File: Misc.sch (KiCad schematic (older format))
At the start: 18 parts, among them U3 PCF8523TK, U4 TLV70218DBV, U5 CDCE913PW, U7 LM75BDP, U8 LM75BDP, X1 32768, X2 20MHz

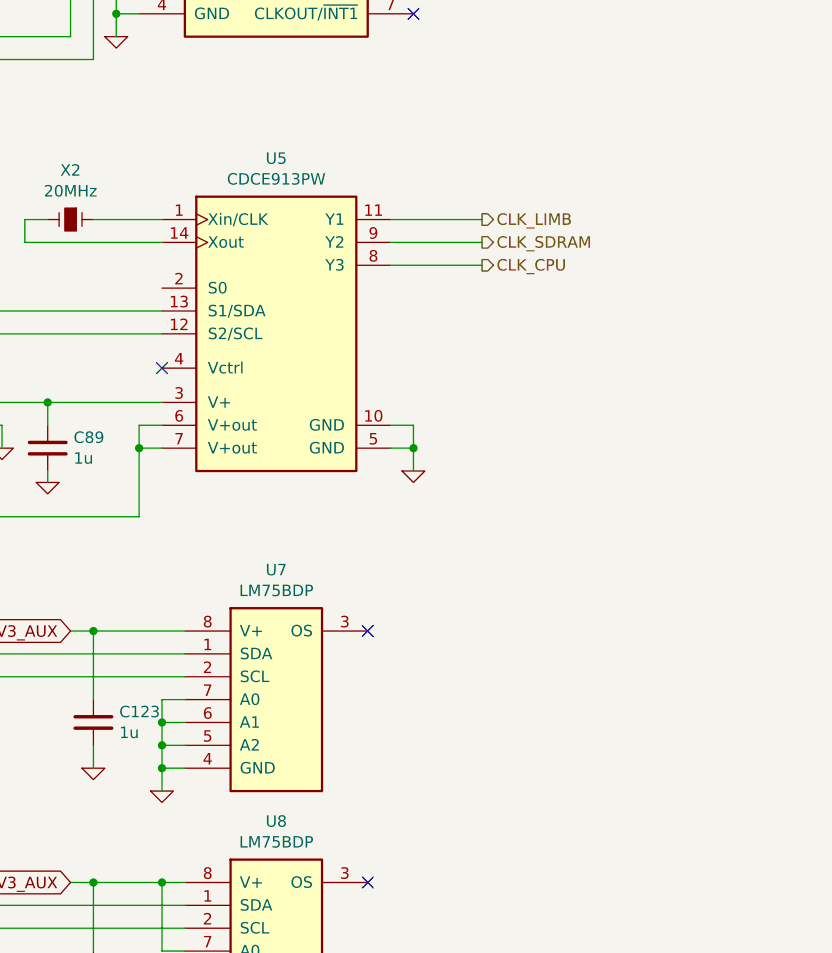
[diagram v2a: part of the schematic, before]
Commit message: Route clocks
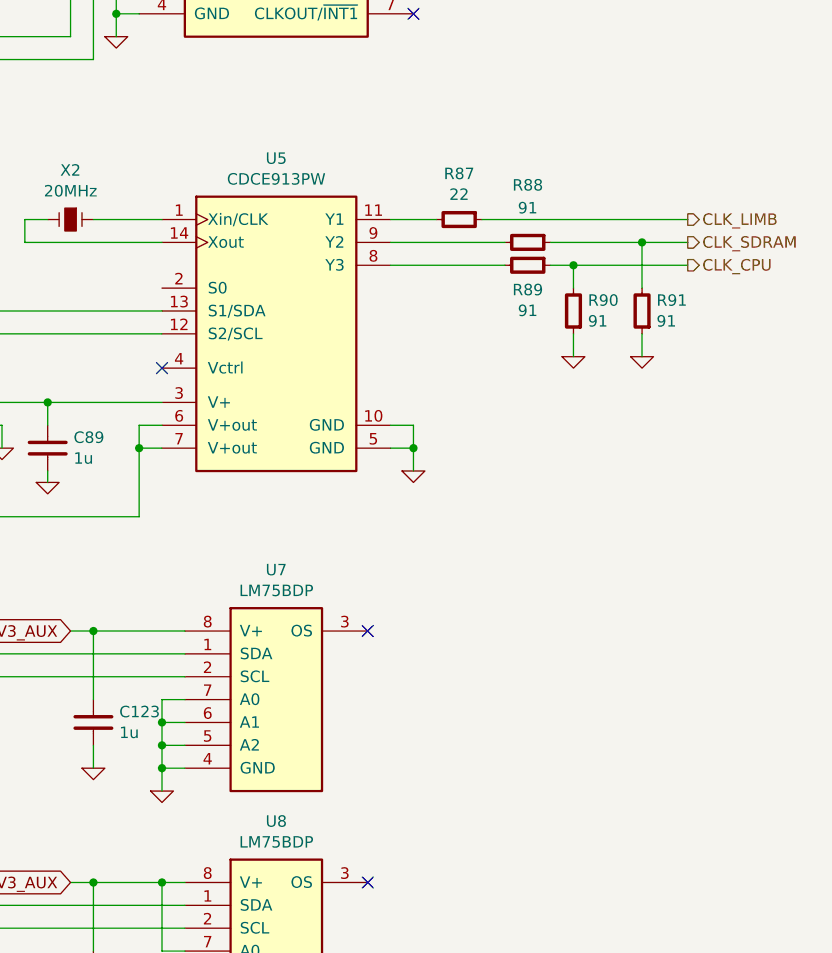
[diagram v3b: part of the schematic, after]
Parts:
- added R87: 22, IPC7351-Nominal:RESC1005X40, symbol R-0402
- added R88, R89, R90, R91: 91, IPC7351-Nominal:RESC1005X40, symbol R-0402
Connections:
- net CLK_CPU: now also R89.1, R90.2; no longer U5.8 (Y3)
- net CLK_LIMB: now also R87.1; no longer U5.11 (Y1)
- net CLK_SDRAM: now also R88.1, R91.2; no longer U5.9 (Y2)
- net GND: now also R90.1, R91.1
- new net: R87.2, U5.11 (Y1)
- new net: R89.2, U5.8 (Y3)
- new net: R88.2, U5.9 (Y2)
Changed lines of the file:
@@
 $Descr A4 11693 8268
 encoding utf-8
-Sheet 10 10
+Sheet 9 10
 Title ""
 Date ""
@@
 Connection ~ 4900 2100
 $Comp
-L GND #PWR176
+L GND #PWR174
 U 1 1 57981F37
 P 4900 2200
-F 0 "#PWR176" H 4900 2200 30  0001 C CNN
+F 0 "#PWR174" H 4900 2200 30  0001 C CNN
 F 1 "GND" H 4900 2130 30  0001 C CNN
 F 2 "" H 4900 2200 60  0000 C CNN
@@
 	6700 1500 6700 1600
 $Comp
-L GND #PWR180
+L GND #PWR178
 U 1 1 57983039
 P 6850 1700
-F 0 "#PWR180" H 6850 1700 30  0001 C CNN
+F 0 "#PWR178" H 6850 1700 30  0001 C CNN
 F 1 "GND" H 6850 1630 30  0001 C CNN
 F 2 "" H 6850 1700 60  0000 C CNN
@@
 Connection ~ 2100 1500
 $Comp
-L GND #PWR164
+L GND #PWR162
 U 1 1 57985104
 P 2100 1850
-F 0 "#PWR164" H 2100 1850 30  0001 C CNN
+F 0 "#PWR162" H 2100 1850 30  0001 C CNN
 F 1 "GND" H 2100 1780 30  0001 C CNN
 F 2 "" H 2100 1850 60  0000 C CNN
@@
 	2100 1850 2100 1800
 $Comp
-L GND #PWR165
+L GND #PWR163
 U 1 1 57985148
 P 2450 1850
-F 0 "#PWR165" H 2450 1850 30  0001 C CNN
+F 0 "#PWR163" H 2450 1850 30  0001 C CNN
 F 1 "GND" H 2450 1780 30  0001 C CNN
 F 2 "" H 2450 1850 60  0000 C CNN
@@
 	2450 1850 2450 1800
 $Comp
-L GND #PWR166
+L GND #PWR164
 U 1 1 5798515D
 P 2800 1850
-F 0 "#PWR166" H 2800 1850 30  0001 C CNN
+F 0 "#PWR164" H 2800 1850 30  0001 C CNN
 F 1 "GND" H 2800 1780 30  0001 C CNN
 F 2 "" H 2800 1850 60  0000 C CNN
@@
 	2800 1850 2800 1800
 $Comp
-L GND #PWR168
+L GND #PWR166
 U 1 1 57985164
 P 3150 1850
-F 0 "#PWR168" H 3150 1850 30  0001 C CNN
+F 0 "#PWR166" H 3150 1850 30  0001 C CNN
 F 1 "GND" H 3150 1780 30  0001 C CNN
 F 2 "" H 3150 1850 60  0000 C CNN
@@
 	3800 1600 3800 1700
 $Comp
-L GND #PWR170
+L GND #PWR168
 U 1 1 5798538F
 P 3800 2000
-F 0 "#PWR170" H 3800 2000 30  0001 C CNN
+F 0 "#PWR168" H 3800 2000 30  0001 C CNN
 F 1 "GND" H 3800 1930 30  0001 C CNN
 F 2 "" H 3800 2000 60  0000 C CNN
@@
 Connection ~ 4300 1600
 $Comp
-L GND #PWR171
+L GND #PWR169
 U 1 1 5798545A
 P 4300 2000
-F 0 "#PWR171" H 4300 2000 30  0001 C CNN
+F 0 "#PWR169" H 4300 2000 30  0001 C CNN
 F 1 "GND" H 4300 1930 30  0001 C CNN
 F 2 "" H 4300 2000 60  0000 C CNN
@@
 	1    0    0    -1
 $EndComp
-Text HLabel 6500 3000 2    50   Output ~ 0
+Text HLabel 7400 3000 2    50   Output ~ 0
 CLK_LIMB
-Text HLabel 6500 3100 2    50   Output ~ 0
+Text HLabel 7400 3100 2    50   Output ~ 0
 CLK_SDRAM
-Text HLabel 6500 3200 2    50   Output ~ 0
+Text HLabel 7400 3200 2    50   Output ~ 0
 CLK_CPU
-Wire Wire Line
-	6500 3000 6100 3000
-Wire Wire Line
-	6500 3100 6100 3100
-Wire Wire Line
-	6500 3200 6100 3200
-$Comp
-L GND #PWR179
+$Comp
+L GND #PWR177
 U 1 1 5798C21D
 P 6200 4100
-F 0 "#PWR179" H 6200 4100 30  0001 C CNN
+F 0 "#PWR177" H 6200 4100 30  0001 C CNN
 F 1 "GND" H 6200 4030 30  0001 C CNN
 F 2 "" H 6200 4100 60  0000 C CNN
@@
 	4300 3800 5100 3800
 $Comp
-L GND #PWR172
+L GND #PWR170
 U 1 1 5798C570
 P 4400 4000
-F 0 "#PWR172" H 4400 4000 30  0001 C CNN
+F 0 "#PWR170" H 4400 4000 30  0001 C CNN
 F 1 "GND" H 4400 3930 30  0001 C CNN
 F 2 "" H 4400 4000 60  0000 C CNN
@@
 	4400 3900 4300 3900
 $Comp
-L GND #PWR169
+L GND #PWR167
 U 1 1 5798C5E9
 P 3500 4100
-F 0 "#PWR169" H 3500 4100 30  0001 C CNN
+F 0 "#PWR167" H 3500 4100 30  0001 C CNN
 F 1 "GND" H 3500 4030 30  0001 C CNN
 F 2 "" H 3500 4100 60  0000 C CNN
@@
 Connection ~ 3100 3800
 $Comp
-L GND #PWR167
+L GND #PWR165
 U 1 1 5798C8CA
 P 3100 4150
-F 0 "#PWR167" H 3100 4150 30  0001 C CNN
+F 0 "#PWR165" H 3100 4150 30  0001 C CNN
 F 1 "GND" H 3100 4080 30  0001 C CNN
 F 2 "" H 3100 4150 60  0000 C CNN
@@
 Connection ~ 4600 3800
 $Comp
-L GND #PWR173
+L GND #PWR171
 U 1 1 5798C9F9
 P 4600 4150
-F 0 "#PWR173" H 4600 4150 30  0001 C CNN
+F 0 "#PWR171" H 4600 4150 30  0001 C CNN
 F 1 "GND" H 4600 4080 30  0001 C CNN
 F 2 "" H 4600 4150 60  0000 C CNN
@@
 Connection ~ 2300 3500
 $Comp
-L GND #PWR177
+L GND #PWR175
 U 1 1 579F4E8E
 P 5100 5500
-F 0 "#PWR177" H 5100 5500 30  0001 C CNN
+F 0 "#PWR175" H 5100 5500 30  0001 C CNN
 F 1 "GND" H 5100 5430 30  0001 C CNN
 F 2 "" H 5100 5500 60  0000 C CNN
@@
 $EndComp
 Wire Wire Line
-	5100 5500 5100 5100
+	5100 5100 5100 5500
 Wire Wire Line
 	5100 5100 5200 5100
@@
 	5100 6300 5100 6600
 $Comp
-L GND #PWR178
+L GND #PWR176
 U 1 1 579F532E
 P 5100 6600
-F 0 "#PWR178" H 5100 6600 30  0001 C CNN
+F 0 "#PWR176" H 5100 6600 30  0001 C CNN
 F 1 "GND" H 5100 6530 30  0001 C CNN
 F 2 "" H 5100 6600 60  0000 C CNN
@@
 Connection ~ 4800 4800
 $Comp
-L GND #PWR174
+L GND #PWR172
 U 1 1 579F5F9F
 P 4800 5400
-F 0 "#PWR174" H 4800 5400 30  0001 C CNN
+F 0 "#PWR172" H 4800 5400 30  0001 C CNN
 F 1 "GND" H 4800 5330 30  0001 C CNN
 F 2 "" H 4800 5400 60  0000 C CNN
@@
 Connection ~ 4800 5900
 $Comp
-L GND #PWR175
+L GND #PWR173
 U 1 1 579F6133
 P 4800 6500
-F 0 "#PWR175" H 4800 6500 30  0001 C CNN
+F 0 "#PWR173" H 4800 6500 30  0001 C CNN
 F 1 "GND" H 4800 6430 30  0001 C CNN
 F 2 "" H 4800 6500 60  0000 C CNN
@@
 Wire Wire Line
 	4800 6500 4800 6400
+$Comp
+L R-0402 R87
+U 1 1 57A14DBD
+P 6400 3000
+F 0 "R87" V 6200 3000 50  0000 C CNN
+F 1 "22" V 6291 3000 50  0000 C CNN
+F 2 "IPC7351-Nominal:RESC1005X40" H 6400 3000 50  0001 C CNN
+F 3 "" H 6400 3050 60  0000 C CNN
+F 4 "RES SMD 22 1% [0402]" H 7150 3550 60  0001 C CNN "BOM"
+	1    6400 3000
+	0    1    1    0
+$EndComp
+Wire Wire Line
+	6300 3000 6100 3000
+Wire Wire Line
+	6500 3000 7400 3000
+$Comp
+L R-0402 R88
+U 1 1 57A1503E
+P 6700 3100
+F 0 "R88" V 6450 3100 50  0000 C CNN
+F 1 "91" V 6550 3100 50  0000 C CNN
+F 2 "IPC7351-Nominal:RESC1005X40" H 6700 3100 50  0001 C CNN
+F 3 "" H 6700 3150 60  0000 C CNN
+F 4 "RES SMD 91 1% [0402]" H 7450 3650 60  0001 C CNN "BOM"
+	1    6700 3100
+	0    1    1    0
+$EndComp
+Wire Wire Line
+	6600 3100 6100 3100
+Wire Wire Line
+	6800 3100 7400 3100
+$Comp
+L R-0402 R89
+U 1 1 57A152BE
+P 6700 3200
+F 0 "R89" V 6808 3200 50  0000 C CNN
+F 1 "91" V 6899 3200 50  0000 C CNN
+F 2 "IPC7351-Nominal:RESC1005X40" H 6700 3200 50  0001 C CNN
+F 3 "" H 6700 3250 60  0000 C CNN
+F 4 "RES SMD 91 1% [0402]" H 7450 3750 60  0001 C CNN "BOM"
+	1    6700 3200
+	0    1    1    0
+$EndComp
+Wire Wire Line
+	6800 3200 7400 3200
+Wire Wire Line
+	6600 3200 6100 3200
+$Comp
+L R-0402 R90
+U 1 1 57A154AF
+P 6900 3400
+F 0 "R90" H 6837 3354 50  0000 R CNN
+F 1 "91" H 6837 3445 50  0000 R CNN
+F 2 "IPC7351-Nominal:RESC1005X40" H 6900 3400 50  0001 C CNN
+F 3 "" H 6900 3450 60  0000 C CNN
+F 4 "RES SMD 91 1% [0402]" H 7650 3950 60  0001 C CNN "BOM"
+	1    6900 3400
+	-1   0    0    1
+$EndComp
+Wire Wire Line
+	6900 3300 6900 3200
+Connection ~ 6900 3200
+$Comp
+L R-0402 R91
+U 1 1 57A15674
+P 7200 3400
+F 0 "R91" H 7137 3354 50  0000 R CNN
+F 1 "91" H 7137 3445 50  0000 R CNN
+F 2 "IPC7351-Nominal:RESC1005X40" H 7200 3400 50  0001 C CNN
+F 3 "" H 7200 3450 60  0000 C CNN
+F 4 "RES SMD 91 1% [0402]" H 7950 3950 60  0001 C CNN "BOM"
+	1    7200 3400
+	-1   0    0    1
+$EndComp
+Wire Wire Line
+	7200 3300 7200 3100
+Connection ~ 7200 3100
+$Comp
+L GND #PWR179
+U 1 1 57A157A8
+P 6900 3600
+F 0 "#PWR179" H 6900 3600 30  0001 C CNN
+F 1 "GND" H 6900 3530 30  0001 C CNN
+F 2 "" H 6900 3600 60  0000 C CNN
+F 3 "" H 6900 3600 60  0000 C CNN
+	1    6900 3600
+	1    0    0    -1
+$EndComp
+Wire Wire Line
+	6900 3600 6900 3500
+$Comp
+L GND #PWR180
+U 1 1 57A158A4
+P 7200 3600
+F 0 "#PWR180" H 7200 3600 30  0001 C CNN
+F 1 "GND" H 7200 3530 30  0001 C CNN
+F 2 "" H 7200 3600 60  0000 C CNN
+F 3 "" H 7200 3600 60  0000 C CNN
+	1    7200 3600
+	1    0    0    -1
+$EndComp
+Wire Wire Line
+	7200 3600 7200 3500
 $EndSCHEMATC

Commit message: Proper coin cell holder
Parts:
- BT1: footprint (none) -> manuf:MPD-BU2032SM-HD-G
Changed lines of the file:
@@
 F 0 "BT1" H 3940 1821 50  0000 L CNN
 F 1 "3V" H 3940 1730 50  0000 L CNN
-F 2 "" H 3800 1700 60  0000 C CNN
+F 2 "manuf:MPD-BU2032SM-HD-G" H 3800 1700 60  0001 C CNN
 F 3 "" H 3800 1700 60  0000 C CNN
 F 4 "DIST DIGIKEY BU2032SM-HD-GCT-ND" H 3800 1800 60  0001 C CNN "BOM"

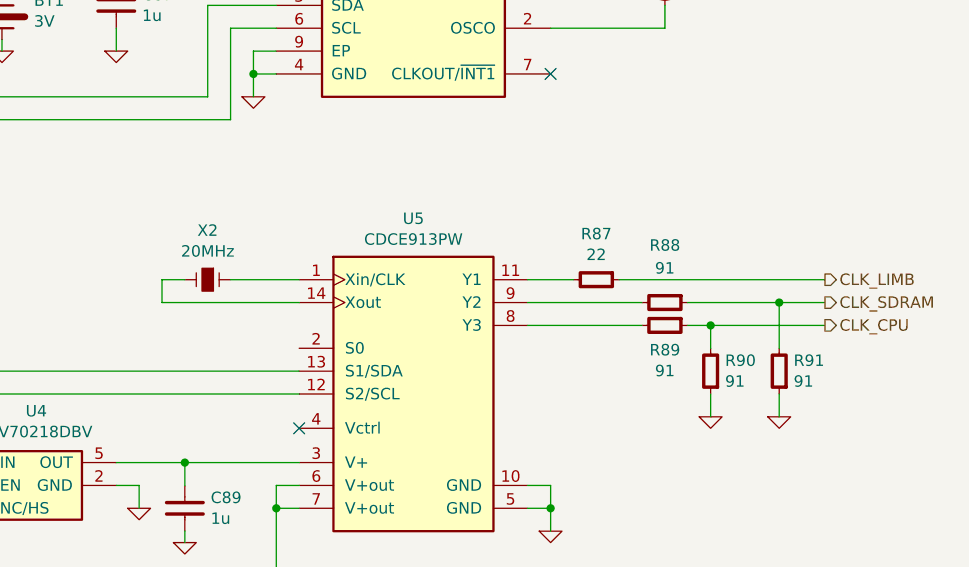
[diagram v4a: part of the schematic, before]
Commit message: Add RS-232
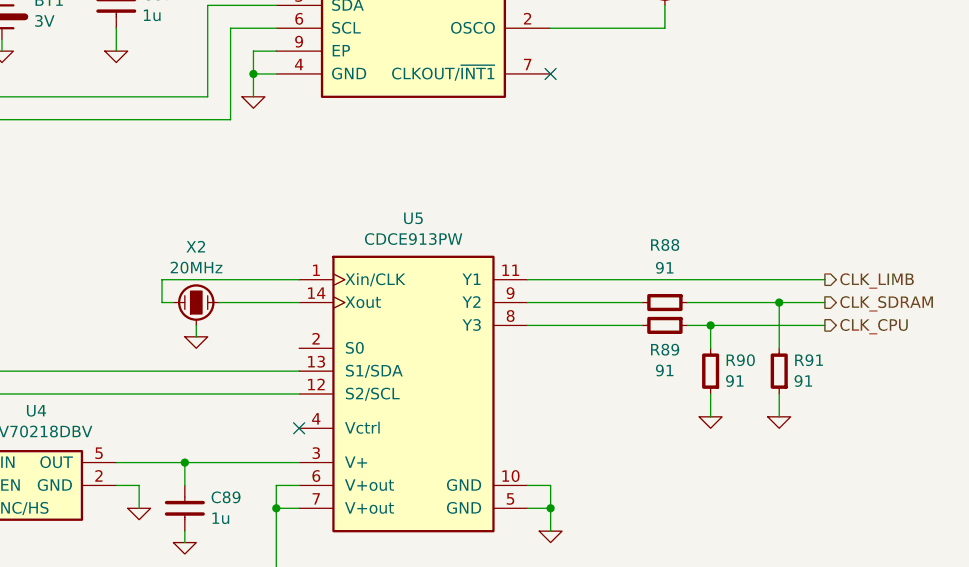
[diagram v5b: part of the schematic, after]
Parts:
- removed R87: 22, IPC7351-Nominal:RESC1005X40, symbol R-0402
- removed X2: 20MHz, IPC7351-Nominal:XTAL1200X480X460, symbol XTAL-HC49US-SMD
- added X2: 20MHz, manuf:ABRACON-ABM8G, symbol XTAL-ABRACON-ABM8G
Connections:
- net CLK_LIMB: now also U5.11 (Y1)
- net GND: now also X2.3
- net at U5.1 (Xin/CLK): now also X2.1
- net at U5.14 (Xout): now also X2.2
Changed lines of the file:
@@
 Connection ~ 4900 2100
 $Comp
-L GND #PWR174
+L GND #PWR183
 U 1 1 57981F37
 P 4900 2200
-F 0 "#PWR174" H 4900 2200 30  0001 C CNN
+F 0 "#PWR183" H 4900 2200 30  0001 C CNN
 F 1 "GND" H 4900 2130 30  0001 C CNN
 F 2 "" H 4900 2200 60  0000 C CNN
@@
 	6700 1500 6700 1600
 $Comp
-L GND #PWR178
+L GND #PWR187
 U 1 1 57983039
 P 6850 1700
-F 0 "#PWR178" H 6850 1700 30  0001 C CNN
+F 0 "#PWR187" H 6850 1700 30  0001 C CNN
 F 1 "GND" H 6850 1630 30  0001 C CNN
 F 2 "" H 6850 1700 60  0000 C CNN
@@
 Connection ~ 2100 1500
 $Comp
-L GND #PWR162
+L GND #PWR170
 U 1 1 57985104
 P 2100 1850
-F 0 "#PWR162" H 2100 1850 30  0001 C CNN
+F 0 "#PWR170" H 2100 1850 30  0001 C CNN
 F 1 "GND" H 2100 1780 30  0001 C CNN
 F 2 "" H 2100 1850 60  0000 C CNN
@@
 	2100 1850 2100 1800
 $Comp
-L GND #PWR163
+L GND #PWR171
 U 1 1 57985148
 P 2450 1850
-F 0 "#PWR163" H 2450 1850 30  0001 C CNN
+F 0 "#PWR171" H 2450 1850 30  0001 C CNN
 F 1 "GND" H 2450 1780 30  0001 C CNN
 F 2 "" H 2450 1850 60  0000 C CNN
@@
 	2450 1850 2450 1800
 $Comp
-L GND #PWR164
+L GND #PWR172
 U 1 1 5798515D
 P 2800 1850
-F 0 "#PWR164" H 2800 1850 30  0001 C CNN
+F 0 "#PWR172" H 2800 1850 30  0001 C CNN
 F 1 "GND" H 2800 1780 30  0001 C CNN
 F 2 "" H 2800 1850 60  0000 C CNN
@@
 	2800 1850 2800 1800
 $Comp
-L GND #PWR166
+L GND #PWR174
 U 1 1 57985164
 P 3150 1850
-F 0 "#PWR166" H 3150 1850 30  0001 C CNN
+F 0 "#PWR174" H 3150 1850 30  0001 C CNN
 F 1 "GND" H 3150 1780 30  0001 C CNN
 F 2 "" H 3150 1850 60  0000 C CNN
@@
 	3800 1600 3800 1700
 $Comp
-L GND #PWR168
+L GND #PWR176
 U 1 1 5798538F
 P 3800 2000
-F 0 "#PWR168" H 3800 2000 30  0001 C CNN
+F 0 "#PWR176" H 3800 2000 30  0001 C CNN
 F 1 "GND" H 3800 1930 30  0001 C CNN
 F 2 "" H 3800 2000 60  0000 C CNN
@@
 Connection ~ 4300 1600
 $Comp
-L GND #PWR169
+L GND #PWR177
 U 1 1 5798545A
 P 4300 2000
-F 0 "#PWR169" H 4300 2000 30  0001 C CNN
+F 0 "#PWR177" H 4300 2000 30  0001 C CNN
 F 1 "GND" H 4300 1930 30  0001 C CNN
 F 2 "" H 4300 2000 60  0000 C CNN
@@
 CLK_CPU
 $Comp
-L GND #PWR177
+L GND #PWR186
 U 1 1 5798C21D
 P 6200 4100
-F 0 "#PWR177" H 6200 4100 30  0001 C CNN
+F 0 "#PWR186" H 6200 4100 30  0001 C CNN
 F 1 "GND" H 6200 4030 30  0001 C CNN
 F 2 "" H 6200 4100 60  0000 C CNN
@@
 	6200 4000 6100 4000
 Connection ~ 6200 4000
-$Comp
-L XTAL-HC49US-SMD X2
-U 1 1 5798C2EB
-P 4700 3000
-F 0 "X2" V 4485 3000 50  0000 C CNN
-F 1 "20MHz" V 4576 3000 50  0000 C CNN
-F 2 "IPC7351-Nominal:XTAL1200X480X460" H 4800 2950 60  0001 C CNN
-F 3 "" H 4700 3000 60  0000 C CNN
-	1    4700 3000
-	0    1    1    0
-$EndComp
-Wire Wire Line
-	4800 3000 5100 3000
-Wire Wire Line
-	5100 3100 4500 3100
 Wire Wire Line
 	4500 3100 4500 3000
 Wire Wire Line
-	4500 3000 4600 3000
+	4500 3000 5100 3000
 Wire Wire Line
 	2400 3400 5100 3400
@@
 	4300 3800 5100 3800
 $Comp
-L GND #PWR170
+L GND #PWR178
 U 1 1 5798C570
 P 4400 4000
-F 0 "#PWR170" H 4400 4000 30  0001 C CNN
+F 0 "#PWR178" H 4400 4000 30  0001 C CNN
 F 1 "GND" H 4400 3930 30  0001 C CNN
 F 2 "" H 4400 4000 60  0000 C CNN
@@
 	4400 3900 4300 3900
 $Comp
-L GND #PWR167
+L GND #PWR175
 U 1 1 5798C5E9
 P 3500 4100
-F 0 "#PWR167" H 3500 4100 30  0001 C CNN
+F 0 "#PWR175" H 3500 4100 30  0001 C CNN
 F 1 "GND" H 3500 4030 30  0001 C CNN
 F 2 "" H 3500 4100 60  0000 C CNN
@@
 Connection ~ 3100 3800
 $Comp
-L GND #PWR165
+L GND #PWR173
 U 1 1 5798C8CA
 P 3100 4150
-F 0 "#PWR165" H 3100 4150 30  0001 C CNN
+F 0 "#PWR173" H 3100 4150 30  0001 C CNN
 F 1 "GND" H 3100 4080 30  0001 C CNN
 F 2 "" H 3100 4150 60  0000 C CNN
@@
 Connection ~ 4600 3800
 $Comp
-L GND #PWR171
+L GND #PWR179
 U 1 1 5798C9F9
 P 4600 4150
-F 0 "#PWR171" H 4600 4150 30  0001 C CNN
+F 0 "#PWR179" H 4600 4150 30  0001 C CNN
 F 1 "GND" H 4600 4080 30  0001 C CNN
 F 2 "" H 4600 4150 60  0000 C CNN
@@
 Connection ~ 2300 3500
 $Comp
-L GND #PWR175
+L GND #PWR184
 U 1 1 579F4E8E
 P 5100 5500
-F 0 "#PWR175" H 5100 5500 30  0001 C CNN
+F 0 "#PWR184" H 5100 5500 30  0001 C CNN
 F 1 "GND" H 5100 5430 30  0001 C CNN
 F 2 "" H 5100 5500 60  0000 C CNN
@@
 	5100 6300 5100 6600
 $Comp
-L GND #PWR176
+L GND #PWR185
 U 1 1 579F532E
 P 5100 6600
-F 0 "#PWR176" H 5100 6600 30  0001 C CNN
+F 0 "#PWR185" H 5100 6600 30  0001 C CNN
 F 1 "GND" H 5100 6530 30  0001 C CNN
 F 2 "" H 5100 6600 60  0000 C CNN
@@
 Connection ~ 4800 4800
 $Comp
-L GND #PWR172
+L GND #PWR181
 U 1 1 579F5F9F
 P 4800 5400
-F 0 "#PWR172" H 4800 5400 30  0001 C CNN
+F 0 "#PWR181" H 4800 5400 30  0001 C CNN
 F 1 "GND" H 4800 5330 30  0001 C CNN
 F 2 "" H 4800 5400 60  0000 C CNN
@@
 Connection ~ 4800 5900
 $Comp
-L GND #PWR173
+L GND #PWR182
 U 1 1 579F6133
 P 4800 6500
-F 0 "#PWR173" H 4800 6500 30  0001 C CNN
+F 0 "#PWR182" H 4800 6500 30  0001 C CNN
 F 1 "GND" H 4800 6430 30  0001 C CNN
 F 2 "" H 4800 6500 60  0000 C CNN
@@
 Wire Wire Line
 	4800 6500 4800 6400
-$Comp
-L R-0402 R87
-U 1 1 57A14DBD
-P 6400 3000
-F 0 "R87" V 6200 3000 50  0000 C CNN
-F 1 "22" V 6291 3000 50  0000 C CNN
-F 2 "IPC7351-Nominal:RESC1005X40" H 6400 3000 50  0001 C CNN
-F 3 "" H 6400 3050 60  0000 C CNN
-F 4 "RES SMD 22 1% [0402]" H 7150 3550 60  0001 C CNN "BOM"
-	1    6400 3000
-	0    1    1    0
-$EndComp
-Wire Wire Line
-	6300 3000 6100 3000
-Wire Wire Line
-	6500 3000 7400 3000
+Wire Wire Line
+	6100 3000 7400 3000
 $Comp
 L R-0402 R88
@@
 Connection ~ 7200 3100
 $Comp
-L GND #PWR179
+L GND #PWR188
 U 1 1 57A157A8
 P 6900 3600
-F 0 "#PWR179" H 6900 3600 30  0001 C CNN
+F 0 "#PWR188" H 6900 3600 30  0001 C CNN
 F 1 "GND" H 6900 3530 30  0001 C CNN
 F 2 "" H 6900 3600 60  0000 C CNN
@@
 	6900 3600 6900 3500
 $Comp
-L GND #PWR180
+L GND #PWR189
 U 1 1 57A158A4
 P 7200 3600
-F 0 "#PWR180" H 7200 3600 30  0001 C CNN
+F 0 "#PWR189" H 7200 3600 30  0001 C CNN
 F 1 "GND" H 7200 3530 30  0001 C CNN
 F 2 "" H 7200 3600 60  0000 C CNN
@@
 Wire Wire Line
 	7200 3600 7200 3500
+$Comp
+L XTAL-ABRACON-ABM8G X2
+U 1 1 57A1738B
+P 4650 3100
+F 0 "X2" V 4892 3100 50  0000 C CNN
+F 1 "20MHz" V 4801 3100 50  0000 C CNN
+F 2 "manuf:ABRACON-ABM8G" H 4650 2950 60  0001 C CNN
+F 3 "http://www.abracon.com/Resonators/ABM8G.pdf" H 4650 3100 50  0001 C CNN
+F 4 "DIST DIGIKEY 535-10271-1-ND" H 4650 3100 60  0001 C CNN "BOM"
+	1    4650 3100
+	0    -1   -1   0
+$EndComp
+Wire Wire Line
+	4550 3100 4500 3100
+Wire Wire Line
+	4750 3100 5100 3100
+$Comp
+L GND #PWR180
+U 1 1 57A177C2
+P 4650 3250
+F 0 "#PWR180" H 4650 3250 30  0001 C CNN
+F 1 "GND" H 4650 3180 30  0001 C CNN
+F 2 "" H 4650 3250 60  0000 C CNN
+F 3 "" H 4650 3250 60  0000 C CNN
+	1    4650 3250
+	1    0    0    -1
+$EndComp
+Wire Wire Line
+	4650 3250 4650 3200
 $EndSCHEMATC
